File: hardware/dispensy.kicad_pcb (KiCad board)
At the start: 2 copper layers, 125 x 90 mm, 96 parts, among them SW1 BOOTSEL, SW2 RESET, SW3 UP, SW4 MENU, SW5 DOWN, U1 DBT50G-7_62-4P, U10 RP2040, U11 SS54_C22452, U12 SS54_C22452, U13 CAN_IO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

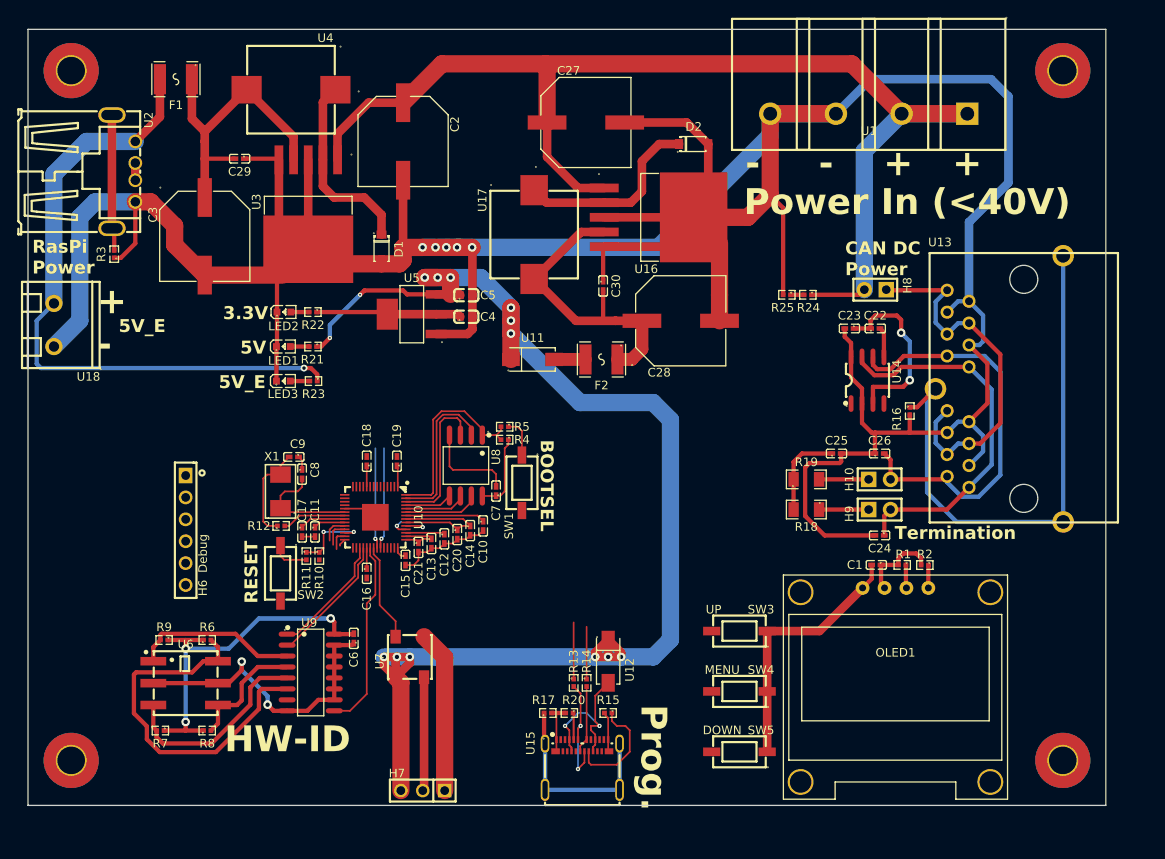
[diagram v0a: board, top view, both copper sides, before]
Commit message: bunch more routing of power and signals
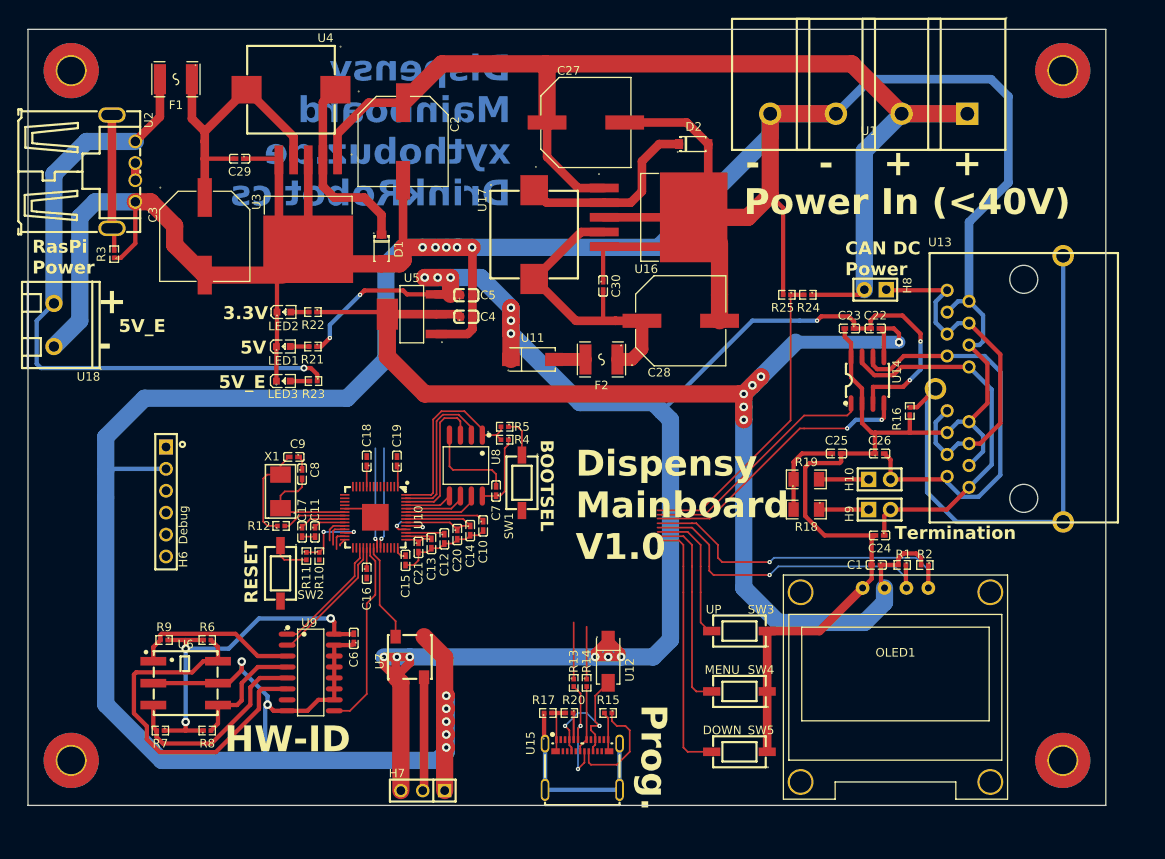
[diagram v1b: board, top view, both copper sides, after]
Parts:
- moved H6 4.02 mm to (109.5, 102.5)
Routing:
- net GND: track 552.0 -> 702.4 mm, vias 7 -> 12
- net +3.3V: track 117.0 -> 237.6 mm, vias 3 -> 9
- net /PI/I2C_SDA: track 2.67 -> 39.7 mm, vias 0 -> 1
- net /PI/I2C_SCL: track 2.70 -> 37.7 mm, vias 0 -> 1
- net /PI/ADC0: track 1.57 -> 35.9 mm
- net Net-(U10-GPIO25): track 11.7 -> 44.5 mm, vias 1 -> 3
- net /PI/IO13: track 0.00 -> 30.2 mm
- net +5V: track 185.4 -> 214.7 mm, vias 16 -> 17
- net Net-(U10-GPIO24): track 11.6 -> 40.0 mm
- net /PI/IO14: track 0.00 -> 23.4 mm
- net /PI/IO15: track 0.00 -> 16.3 mm
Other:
- board text added: "Dispensy Mainboard V1.0"
- board text added: "Dispensy Mainboard xythobuz.de DrinkRobotics"

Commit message: routing nearly finished
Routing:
- net /PI/IO13: track 30.2 -> 80.5 mm, vias 0 -> 2
- net /PI/IO15: track 16.3 -> 55.3 mm, vias 0 -> 2
- net /PI/IO14: track 23.4 -> 60.2 mm, vias 0 -> 2
- net +3.3V: track 237.6 -> 272.3 mm
- net Net-(U10-USB_DM): track 8.11 -> 35.0 mm, vias 1 -> 2
- net /PI/Debug_Clock: track 3.19 -> 29.2 mm
- net /PI/Debug_Data: track 3.03 -> 28.4 mm
- net /PI/Debug_Rx: track 0.93 -> 25.9 mm
- net /PI/Debug_Tx: track 2.39 -> 27.1 mm
- net Net-(U10-USB_DP): track 8.58 -> 31.4 mm, vias 1 -> 2
- net GND: track 702.4 -> 713.9 mm
- net Net-(U10-GPIO24): track 40.0 -> 28.8 mm
- net Net-(U10-GPIO25): track 44.5 -> 33.4 mm
- net /PI/ADC0: track 35.9 -> 34.8 mm
- net /PI/I2C_SCL: track 37.7 -> 37.1 mm

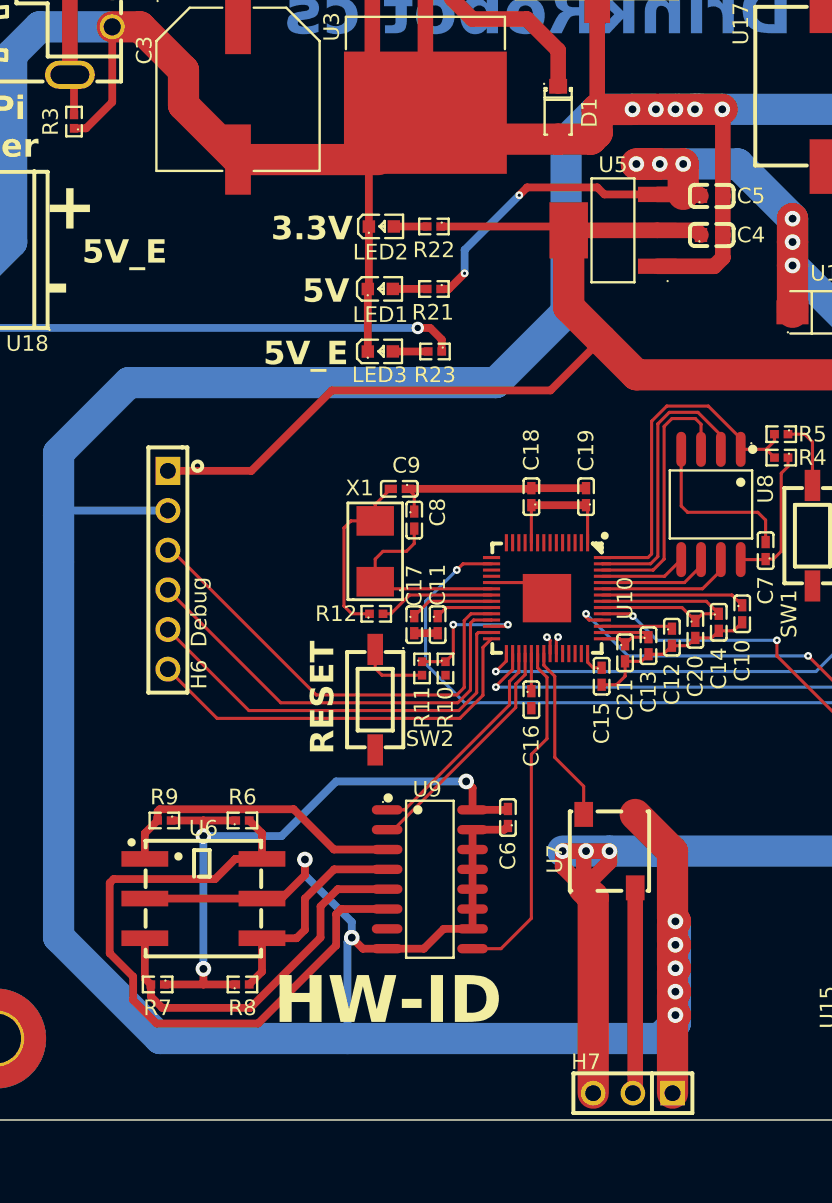
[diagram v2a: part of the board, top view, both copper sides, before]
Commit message: clean up some routes
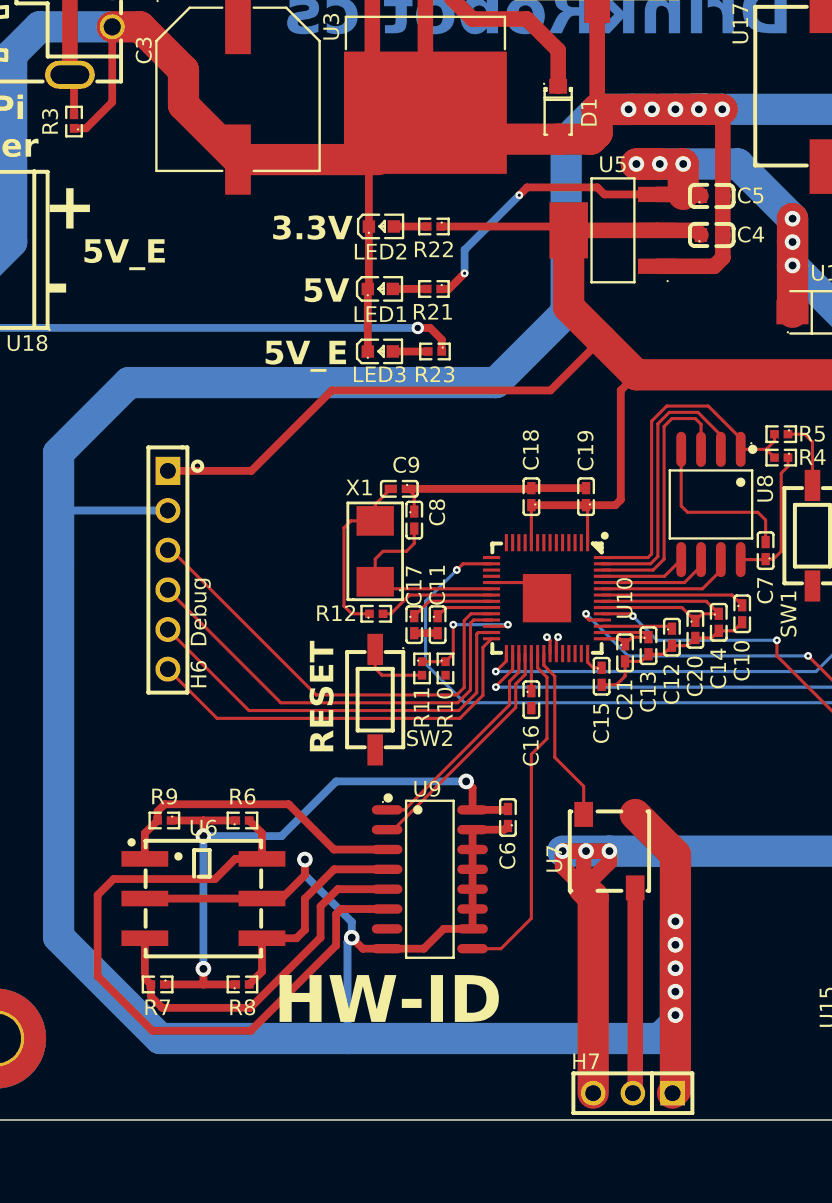
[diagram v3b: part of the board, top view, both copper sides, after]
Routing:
- net +3.3V: track 272.3 -> 283.1 mm
- net Net-(U9-D7): track 42.4 -> 43.9 mm

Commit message: revision 1, date, tweak silkscreen
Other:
- board text added: "Dispensy Mainboard V1 2024-02"
- board text added: "Dispensy Mainboard xythobuz.de DrinkRobotics.de"
- board text removed: "Dispensy Mainboard V1.0"
- board text removed: "Dispensy Mainboard xythobuz.de DrinkRobotics"
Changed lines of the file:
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@@
   (title_block
     (title "Dispensy Mainboard")
-    (date "2024-02-02")
-    (rev "0")
+    (date "2024-02-05")
+    (rev "1")
     (company "DrinkRobotics")
     (comment 1 "https://git.xythobuz.de/thomas/Dispensy")
@@
   (gr_rect (start 93.490456 47.717646) (end 218.490456 137.717646)
     (stroke (width 0.1) (type default)) (fill none) (layer "Edge.Cuts"))
-  (gr_text "Dispensy\nMainboard\nxythobuz.de\nDrinkRobotics" (at 149.5 68.5) (layer "B.Cu")
+  (gr_text "Dispensy\nMainboard\nxythobuz.de\nDrinkRobotics.de" (at 149.5 68.5) (layer "B.Cu")
     (effects (font (size 3 3) (thickness 0.5) bold) (justify left bottom mirror))
   )
@@
     (effects (font (size 3 3) (thickness 0.5) bold) (justify left bottom))
   )
-  (gr_text "Dispensy\nMainboard\nV1.0" (at 157 109.5) (layer "F.SilkS")
+  (gr_text "Dispensy\nMainboard\nV1\n2024-02" (at 157.5 111.5) (layer "F.SilkS")
     (effects (font (size 3 3) (thickness 0.5) bold) (justify left bottom))
   )

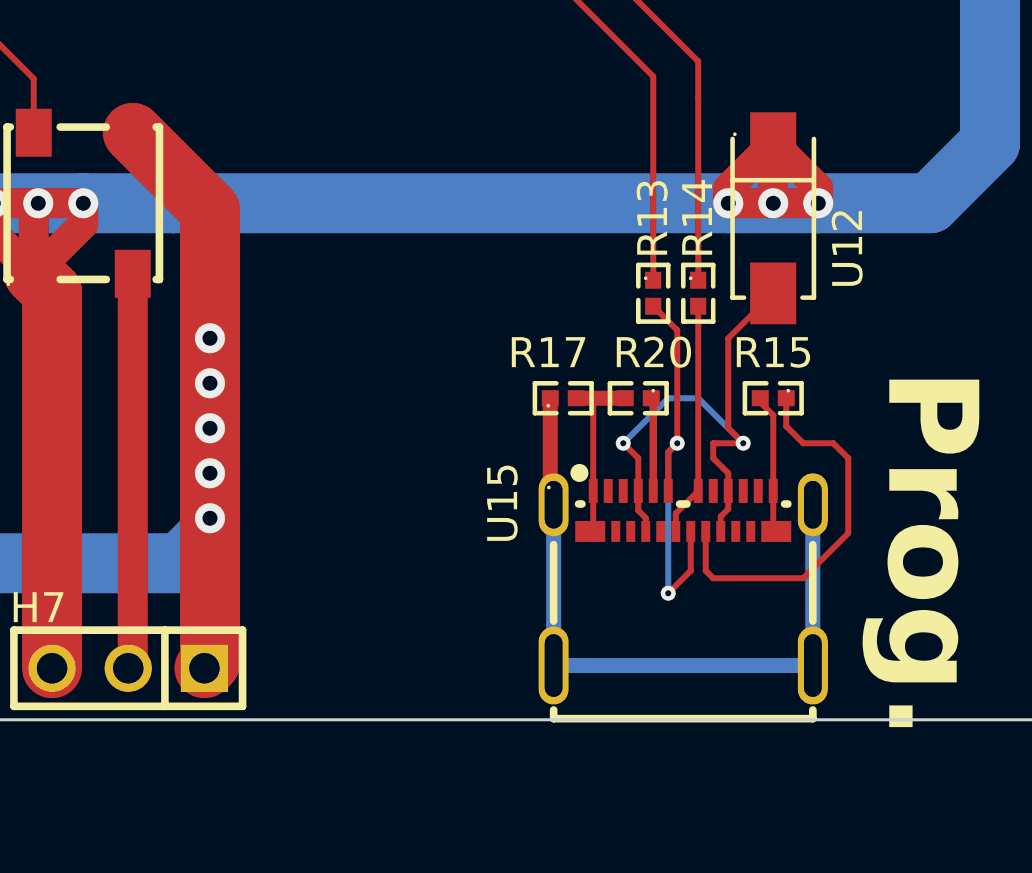
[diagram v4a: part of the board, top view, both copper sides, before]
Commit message: improve usb c routing
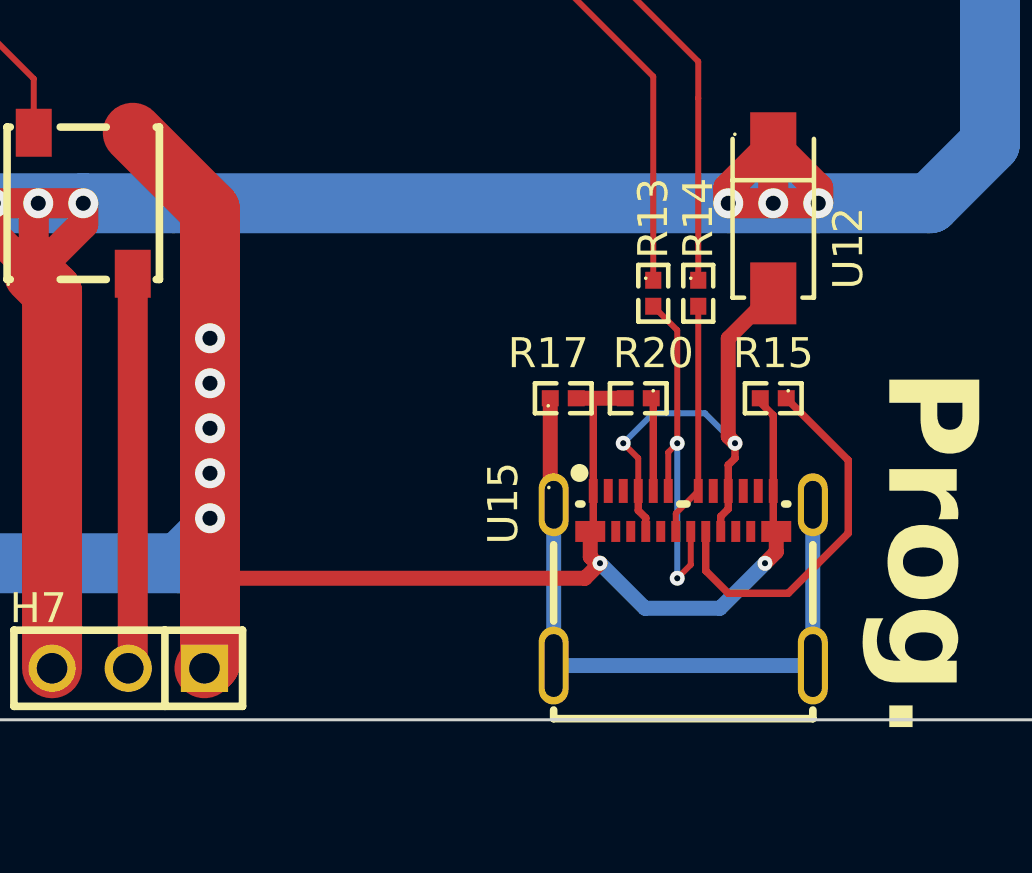
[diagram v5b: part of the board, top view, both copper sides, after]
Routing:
- net GND: track 713.8 -> 736.2 mm, vias 12 -> 14
- net /PI/USBC.VBUS: track 18.6 -> 16.7 mm
- net /PI/USBC.DP: track 14.1 -> 12.9 mm
